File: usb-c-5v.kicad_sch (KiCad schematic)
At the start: 9 parts, among them J2 USB_B_Micro, U2 AP2112K-3.3

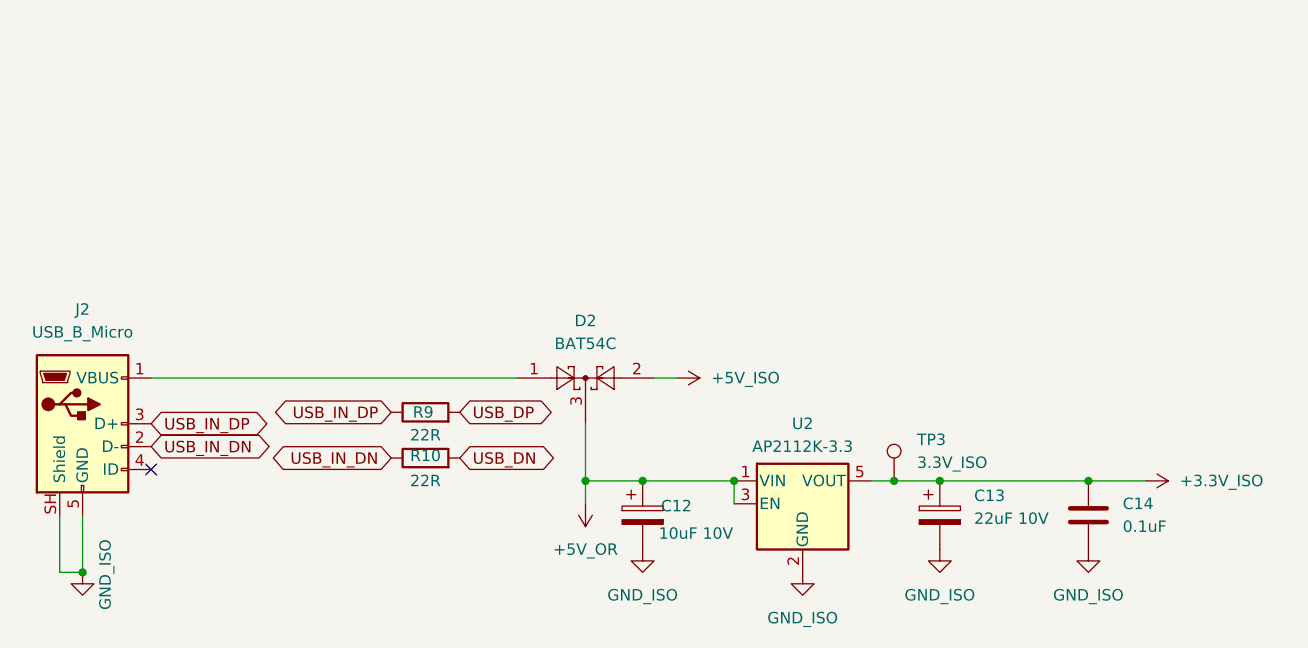
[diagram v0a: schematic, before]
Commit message: Pre-fab QA review fixes: switch input levels, power path, sensor spec, ESD
- R1-R8 switch series resistors 10k -> 1k: with only the ESP32 internal
  ~45k pull-up, 10k divided a closed switch to 0.6V vs the S3's 0.825V
  VIL limit — marginal. 1k gives ~0.1-0.23V worst case.
- U11 ACS723 -> ACS725LLCTR-05AB-T (C3684552): ACS723 needs 4.5-5.5V but
  ran at 3.3V (out of spec). ACS725 is 3.3V-native, same SOIC-8, rated
  to +150C. Firmware: sensitivity 264mV/A, formula (x-1.65)/0.264.
- D2 BAT54C (200mA) removed; replaced with D10/D11 SS34 (3A) diode-OR.
  The old diode carried the full ESP32 load permanently; WiFi TX bursts
  reach 350-500mA.
- U16 PRTR5V0U2X added on USB D+/D- (ESD protection at J2).
- D1 SS34 -> SS54 (5A, same SMA footprint) for multi-motor headroom.
- C10 bumped to 25V-rated 100uF 1210 (C2840614), same footprint.
- Filled all missing LCSC fields for JLCPCB assembly BOM.
- Docs: J4 pinout corrected to as-built; firmware bring-up checklist and
  RTS/DTR terminal gotcha added; CLAUDE.md placement guide for D10/D11/U16.

PCB placement of D10/D11/U16 + F8 sync still pending.

Co-Authored-By: Claude Fable 5 <noreply@anthropic.com>
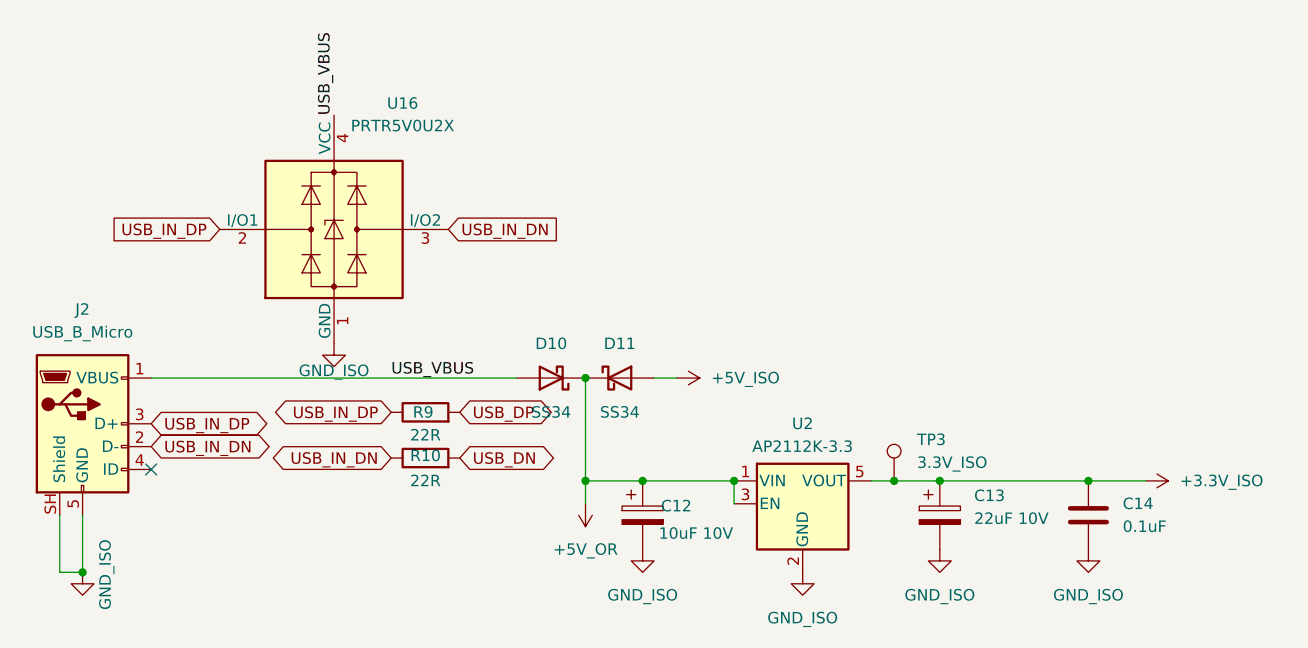
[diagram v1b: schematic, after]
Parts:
- removed D2: BAT54C, Package_TO_SOT_SMD:SOT-23, symbol Diode:BAT54C
- added D10, D11: SS34, Diode_SMD:D_SMA, symbol Diode:SS34
- added U16: PRTR5V0U2X, Package_TO_SOT_SMD:SOT-143, symbol Power_Protection:PRTR5V0U2X
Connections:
- net +5V_ISO: now also D11.2 (A)
- net +5V_OR: now also D10.1 (K), D11.1 (K)
- net GND_ISO: now also U16.1 (GND)
- net USB_IN_DN: now also U16.3 (I/O2)
- net USB_IN_DP: now also U16.2 (I/O1)
- net USB_VBUS: now reaches J2.1 (VBUS)
- net USB_VBUS: now also D10.2 (A), U16.4 (VCC)

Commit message: Rev 1.3 PCB sync + second QA pass: BOM fixes, TVS decoupling, ERC cleanup
PCB (done in KiCad, verified here):
- F8 sync applied: D2 removed; D10/D11 (SS34 SMA) and U16 (PRTR5V0U2X SOT-143)
  placed and routed; R1-R8 -> 1k, D1 -> SS54, C10 -> 25V, U11 -> ACS725 updated
  in place. Footprint-level diff confirms exactly the intended delta, nothing
  else moved. DRC 0 errors / 0 unconnected pads.

Schematic fixes from the second QA pass:
- R1-R8 had NO LCSC part number (value change had landed, part number never
  did) - they would have come back unpopulated, silently killing the switch
  inputs. Set to C14676, matching R14's existing 1K 0603 so it consolidates to
  one BOM line. NOTE: todo.md originally specified C21190 - see the discrepancy
  note there and confirm before ordering.
- TP1-TP7 set in_bom no / in_pos_files no (were 7 junk lines in the JLCPCB BOM).
- Removed 4 orphan dangling wire stubs in switch_inputs.kicad_sch.
- Converted the orphan STBY hierarchical label in motor_drivers.kicad_sch to a
  global label rather than deleting it: its wire actually carried U9 pin 19, so
  deleting dropped U9.19 off the STBY net. Converting keeps the connection and
  clears the ERC hier_label_mismatch.
- Added C40-C43 (100nF 0402, C1525) for U12-U15 VCC decoupling. The switch-input
  TVS devices currently have their nearest +3.3V_ISO bypass 18-23mm away; a
  PRTR5V0U2X shunts ESD into VCC and needs somewhere local to dump it. Still
  need PCB placement - put each within ~2mm of its device's pin 4.

Every schematic edit was validated by diffing the exported netlist before and
after; connectivity is unchanged apart from the four intended new caps.
ERC errors: 10 -> 5 (remaining are 4x missing PWR_FLAG and one J2-GND/U1-(-Vout)
both-power-output pair that is correct by design).

Added barn-blinds-controller.kicad_dru: isolation-barrier audit rule. The board
has no dedicated ISO/MOTOR gap - minimum copper spacing between domains is
0.20mm, the global default. Rev 1.2 measured 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
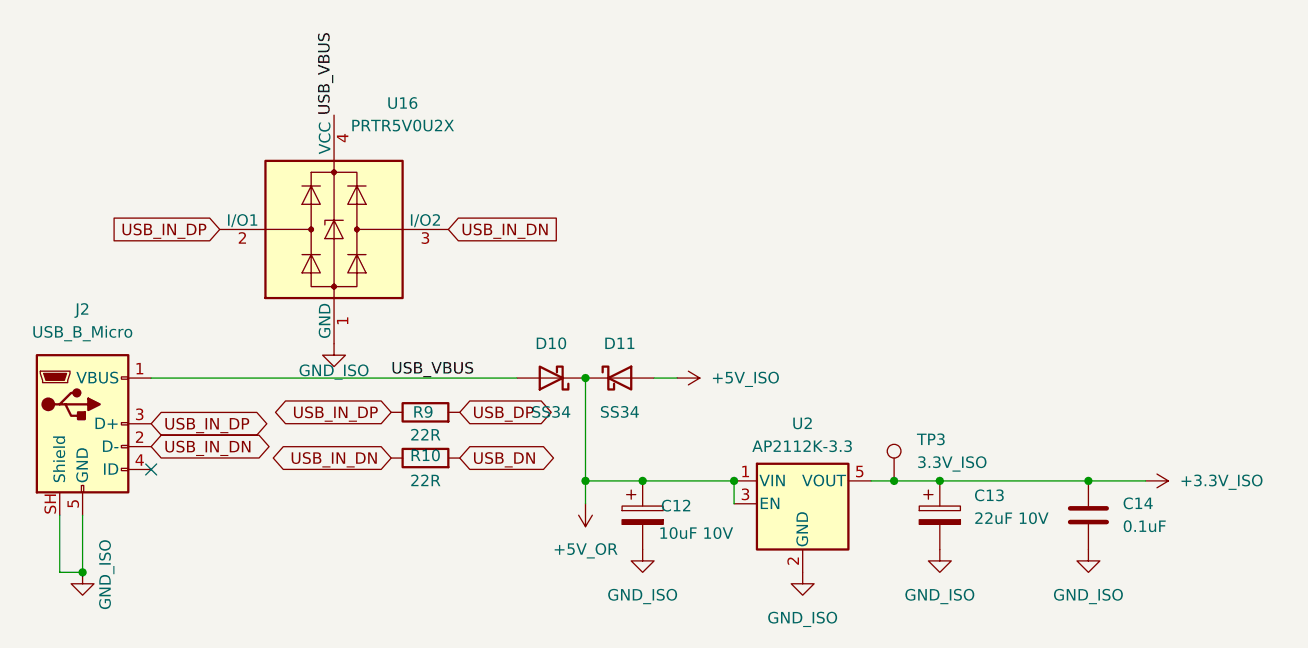
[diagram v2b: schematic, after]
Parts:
- TP3: now left out of the parts list

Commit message: Rev 1.3 fab-ready: PICK UP HERE items closed, JLCPCB production files generated
PCB (verified via DRC/ERC/netlist diff, not just eyeballed):
- Placed C40-C43 within ~1.8-2.6mm of each PRTR5V0U2X VCC pin (U12-U15).
- Widened +5V_OR to 0.5mm and USB_VBUS to 0.4mm.
- Moved U16 closer to J2 (center-to-center 6.1mm -> 4.0mm). Still on B.Cu
  vs J2's F.Cu, so the D+/D- path still crosses layers via a short stub -
  accepted trade-off for a Full-Speed, occasional-use flashing port.
- Fixed D10/D11 silkscreen reference overlap.
- Added LCSC to J2 (C397452, Micro-USB) and J4 (C6652293 - pre-purchased
  JLCPCB inventory part; number is still required for JLCPCB to place it).

DRC: 0 unconnected pads, 0 real errors. Remaining flagged items are all
accepted: 21 isolation-barrier warnings (all >=0.20mm, same floor as Rev 1.2)
and 5 hole_clearance exclusions on J2's own NPTH-vs-pad geometry (footprint-
inherent, not routing-fixable - confirmed the new one is capped by the same
0.20mm pad edge as the pre-existing accepted ones, not by trace width).

ERC steady at 5 benign errors (4x missing PWR_FLAG, 1x J2-GND/U1-(-Vout)
both-power-output by design).

Docs:
- Fixed stale "U7 DCDC DNP" note in jlcpcb-export-steps.md - that referred
  to a pre-renumbering designator. Today U1 is the Heniper DC-DC and U7 is
  a real, actively-used AMS1117-3.3 feeding +3.3V_MOTOR (U4-U6, U8-U9 logic
  supply) that must NOT be DNP'd.
- Documented U1's actual situation instead: DCDC_HYBRID_SLC03_TEC2 is a
  shared THT footprint across three vendor DC-DC modules (Mean Well/Traco/
  Heniper), silkscreened per-hole M/H/T. This run uses the Heniper
  (C20622657, JLCPCB inventory). Same-numbered pads share nets regardless
  of vendor so there's no electrical risk, but BOM/CPL only carry one
  position+rotation for the whole footprint - added a note that the JLCPCB
  assembly order needs an explicit remark to populate only the H holes.
- Updated CLAUDE.md PICK UP HERE and vsp-wsc4-todo.md to reflect fab-ready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
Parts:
- J2: LCSC (none) -> C397452
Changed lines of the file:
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@@
+			)
+		)
+		(property "LCSC" "C397452"
+			(at 45.72 45.72 0)
+			(hide yes)
+			(show_name no)
+			(do_not_autoplace no)
+			(effects
+				(font
+					(size 1.27 1.27)
+				)
 			)
 		)

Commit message: Stock-driven part swaps (C10, U12-U16) + J3 DNP after BOM audit
C10 (isolated 5V_ISO bulk cap): 100uF 25V (C2840614) was out of stock at
JLCPCB. Swapped to 100uF 16V (C7432790, HGC1210R5107M160NSVK) - same 1210
footprint, no PCB rework. 16V chosen over 10V/6.3V alternatives to keep
DC-bias derating low on the ~5V rail (unregulated B1205S-3WR2L output).

U12-U16 (PRTR5V0U2X ESD protection): C12333 was out of stock. Swapped to
C5158049 (UMW/Youtai) - same SOT-143 footprint, no PCB rework. Checked
four other "PRTR5V0U2X"-labeled LCSC listings before picking this one -
they were mismatched (unidirectional, or 14-25V standoff instead of ~5V)
despite sharing the part name; C5158049 actually matches the real
bidirectional/0.35pF/5V-7.2V spec.

Both changes verified via netlist diff (only Value/LCSC fields changed,
zero connectivity impact) and ERC (still 5 known-benign errors).

Auditing the regenerated JLCPCB assembly-order BOM turned up a separate,
pre-existing bug: J3's LCSC (C492404) is a 5-pin header (PZ254V-11-05P),
mismatched against its 7-pin footprint - a leftover from before J3 grew
from 5->7 pins for the RTS/DTR rework, where the LCSC field (and a stale
"01x05" Description) never got updated. JLCPCB's assembly matcher didn't
flag the mismatch, it silently auto-substituted a different 5-pin part.
A real 7-pin replacement isn't in stock either, and J3 is only a backup
UART flashing path (native USB on GPIO19/20 is primary) - not worth
chasing for this run, so J3 is now marked DNP. Fixed the stale "01x05"
Description text to "01x07" so the record is correct if it's ever
un-DNP'd (LCSC still needs a real 7-pin part first if that happens).

PCB: C10/U12-U16 changes synced via F8. J3's new DNP flag still needs an
F8 sync (done after the schematic edit, not yet reflected on the board).

Updated CLAUDE.md PICK UP HERE and vsp-wsc4-todo.md with full detail.
VSP-WSC-4_1.3 production files predate all three changes - needs a
Fabrication Toolkit re-run before ordering.

Co-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
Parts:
- U16: LCSC C12333 -> C5158049
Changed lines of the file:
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@@
 			)
 		)
-		(property "LCSC" "C12333"
+		(property "LCSC" "C5158049"
 			(at 73.66 24.13 0)
 			(hide yes)
